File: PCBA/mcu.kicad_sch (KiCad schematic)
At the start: 13 parts, among them U201 BL604, Y201 40MHz

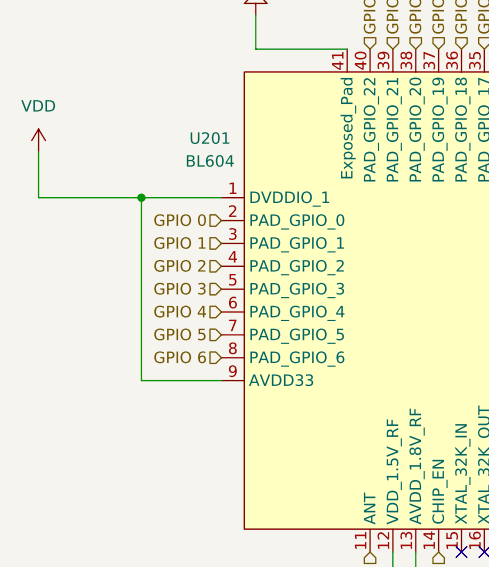
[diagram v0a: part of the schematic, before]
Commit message: Programming uart added
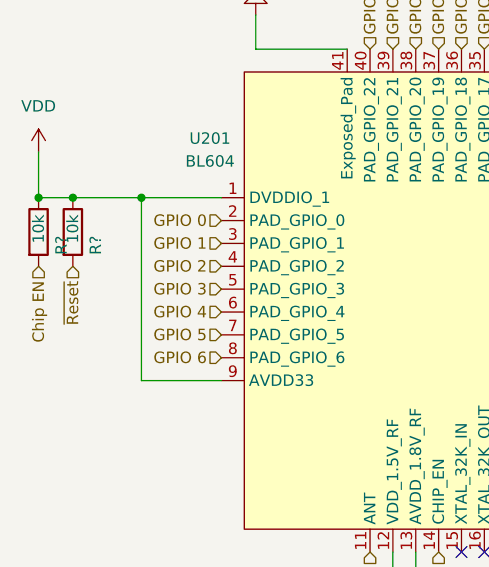
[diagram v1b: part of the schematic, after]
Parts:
- added R? (x2): 10k, Resistor_SMD:R_0603_1608Metric, symbol Device:R
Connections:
- net AVDD33: now also R?.1, R?.1
- net Chip EN: now also R?.2
- net ~{Reset}: now also R?.2
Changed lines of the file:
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@@
   (junction (at 101.6 80.01) (diameter 0) (color 0 0 0 0)
+  )
+  (junction (at 90.17 80.01) (diameter 0) (color 0 0 0 0)
+  )
+  (junction (at 93.98 80.01) (diameter 0) (color 0 0 0 0)
   )
   (junction (at 185.42 114.3) (diameter 0) (color 0 0 0 0)
@@
     (stroke (width 0) (type default) (color 0 0 0 0))
   )
-  (wire (pts (xy 101.6 80.01) (xy 90.17 80.01))
+  (wire (pts (xy 101.6 80.01) (xy 93.98 80.01))
     (stroke (width 0) (type default) (color 0 0 0 0))
   )
@@
   )
   (wire (pts (xy 154.94 63.5) (xy 154.94 55.88))
+    (stroke (width 0) (type default) (color 0 0 0 0))
+  )
+  (wire (pts (xy 93.98 80.01) (xy 90.17 80.01))
     (stroke (width 0) (type default) (color 0 0 0 0))
   )
@@
     (effects (font (size 1.27 1.27)) (justify right))
   )
+  (hierarchical_label "Chip EN" (shape input) (at 90.17 87.63 270)
+    (effects (font (size 1.27 1.27)) (justify right))
+  )
   (hierarchical_label "GPIO 13" (shape input) (at 166.37 87.63 0)
     (effects (font (size 1.27 1.27)) (justify left))
@@
   (hierarchical_label "GPIO 17" (shape input) (at 139.7 63.5 90)
     (effects (font (size 1.27 1.27)) (justify left))
+  )
+  (hierarchical_label "~{Reset}" (shape input) (at 93.98 87.63 270)
+    (effects (font (size 1.27 1.27)) (justify right))
   )
   (hierarchical_label "GPIO 9" (shape input) (at 166.37 97.79 0)
@@
     )
     (property "Datasheet" "~" (id 3) (at 151.13 55.88 0)
+      (effects (font (size 1.27 1.27)) hide)
+    )
+    (pin "1")
+    (pin "2")
+  )
+  (symbol (lib_id "Device:R") (at 93.98 83.82 0) (unit 1)
+    (in_bom yes) (on_board yes)
+    (property "Reference" "R?" (id 0) (at 96.52 86.36 90)
+      (effects (font (size 1.27 1.27)) (justify left))
+    )
+    (property "Value" "10k" (id 1) (at 93.98 85.09 90)
+      (effects (font (size 1.27 1.27)) (justify left))
+    )
+    (property "Footprint" "Resistor_SMD:R_0603_1608Metric" (id 2) (at 92.202 83.82 90)
+      (effects (font (size 1.27 1.27)) hide)
+    )
+    (property "Datasheet" "~" (id 3) (at 93.98 83.82 0)
       (effects (font (size 1.27 1.27)) hide)
     )
@@
       (effects (font (size 1.27 1.27)) hide)
     )
+    (pin "1")
+    (pin "2")
+  )
+  (symbol (lib_id "Device:R") (at 90.17 83.82 0) (unit 1)
+    (in_bom yes) (on_board yes)
+    (property "Reference" "R?" (id 0) (at 92.71 86.36 90)
+      (effects (font (size 1.27 1.27)) (justify left))
+    )
+    (property "Value" "10k" (id 1) (at 90.17 85.09 90)
+      (effects (font (size 1.27 1.27)) (justify left))
+    )
+    (property "Footprint" "Resistor_SMD:R_0603_1608Metric" (id 2) (at 88.392 83.82 90)
+      (effects (font (size 1.27 1.27)) hide)
+    )
+    (property "Datasheet" "~" (id 3) (at 90.17 83.82 0)
+      (effects (font (size 1.27 1.27)) hide)
+    )

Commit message: More schematics
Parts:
- gave numbers to parts that had none: 2
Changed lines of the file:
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@@
   (symbol (lib_id "Device:R") (at 93.98 83.82 0) (unit 1)
     (in_bom yes) (on_board yes)
-    (property "Reference" "R?" (id 0) (at 96.52 86.36 90)
+    (property "Reference" "R203" (id 0) (at 96.52 86.36 90)
       (effects (font (size 1.27 1.27)) (justify left))
     )
@@
   (symbol (lib_id "Device:R") (at 90.17 83.82 0) (unit 1)
     (in_bom yes) (on_board yes)
-    (property "Reference" "R?" (id 0) (at 92.71 86.36 90)
-      (effects (font (size 1.27 1.27)) (justify left))
-    )
+    (property "Reference" "R202" (id 0) (at 92.71 86.36 90)
+      (effects (font (size 1.27 1.27)) (justify left))
+    )

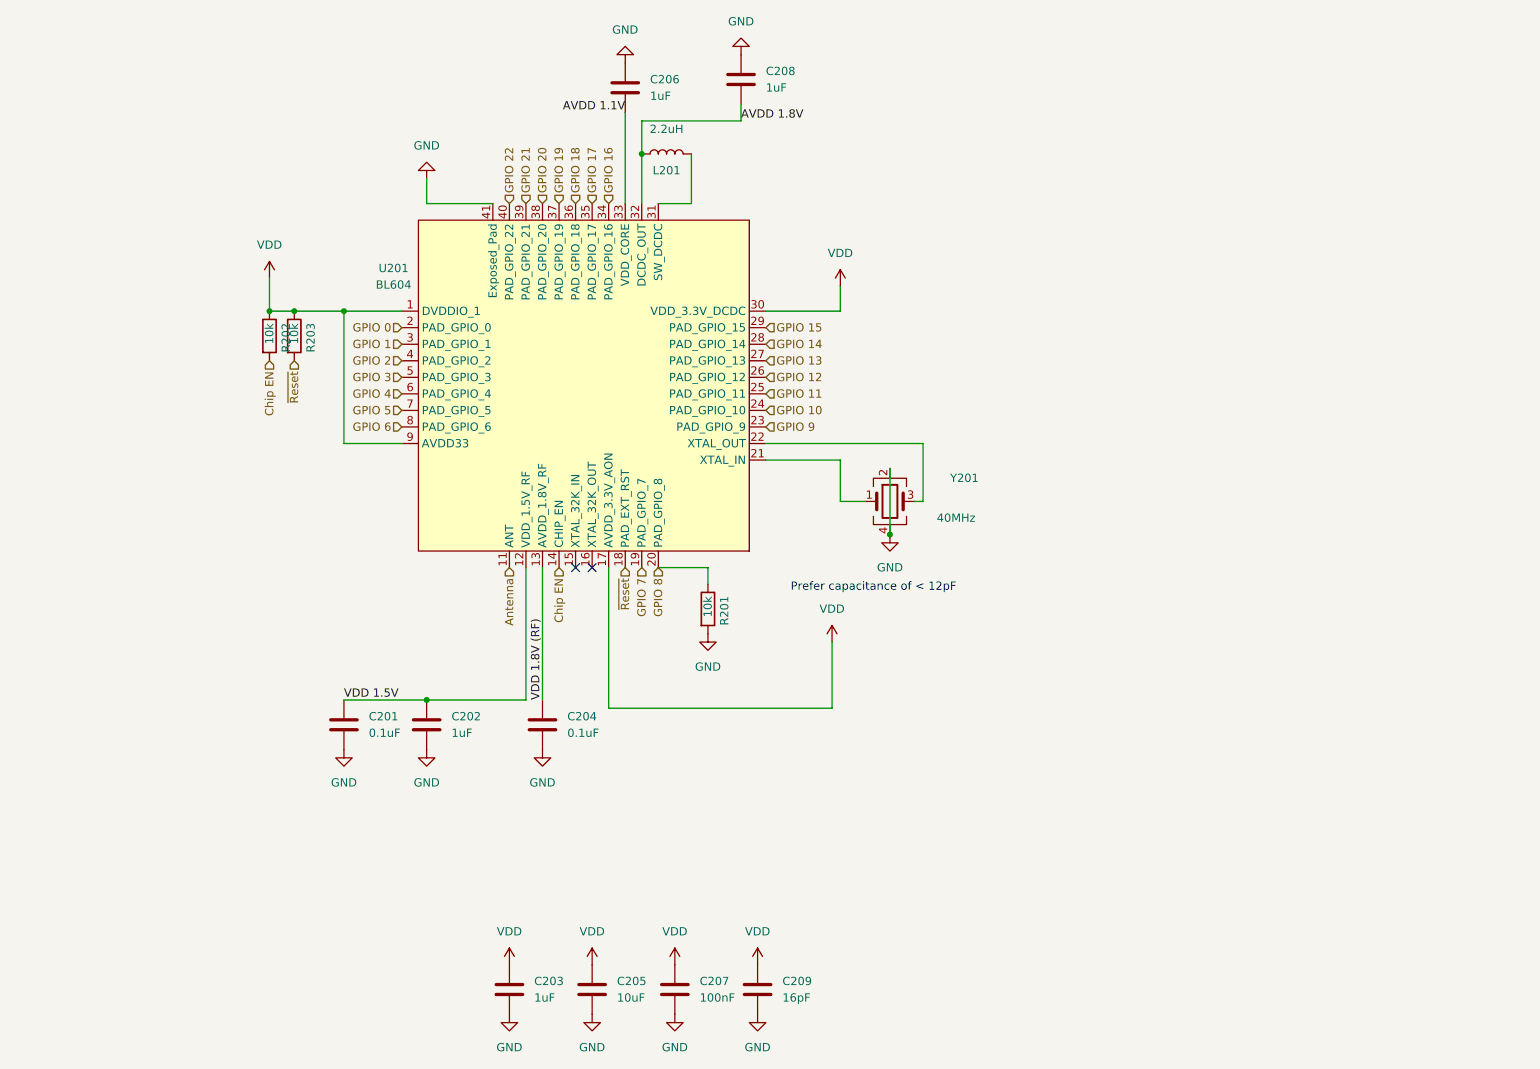
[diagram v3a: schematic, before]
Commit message: Update schematic pinmap bl706
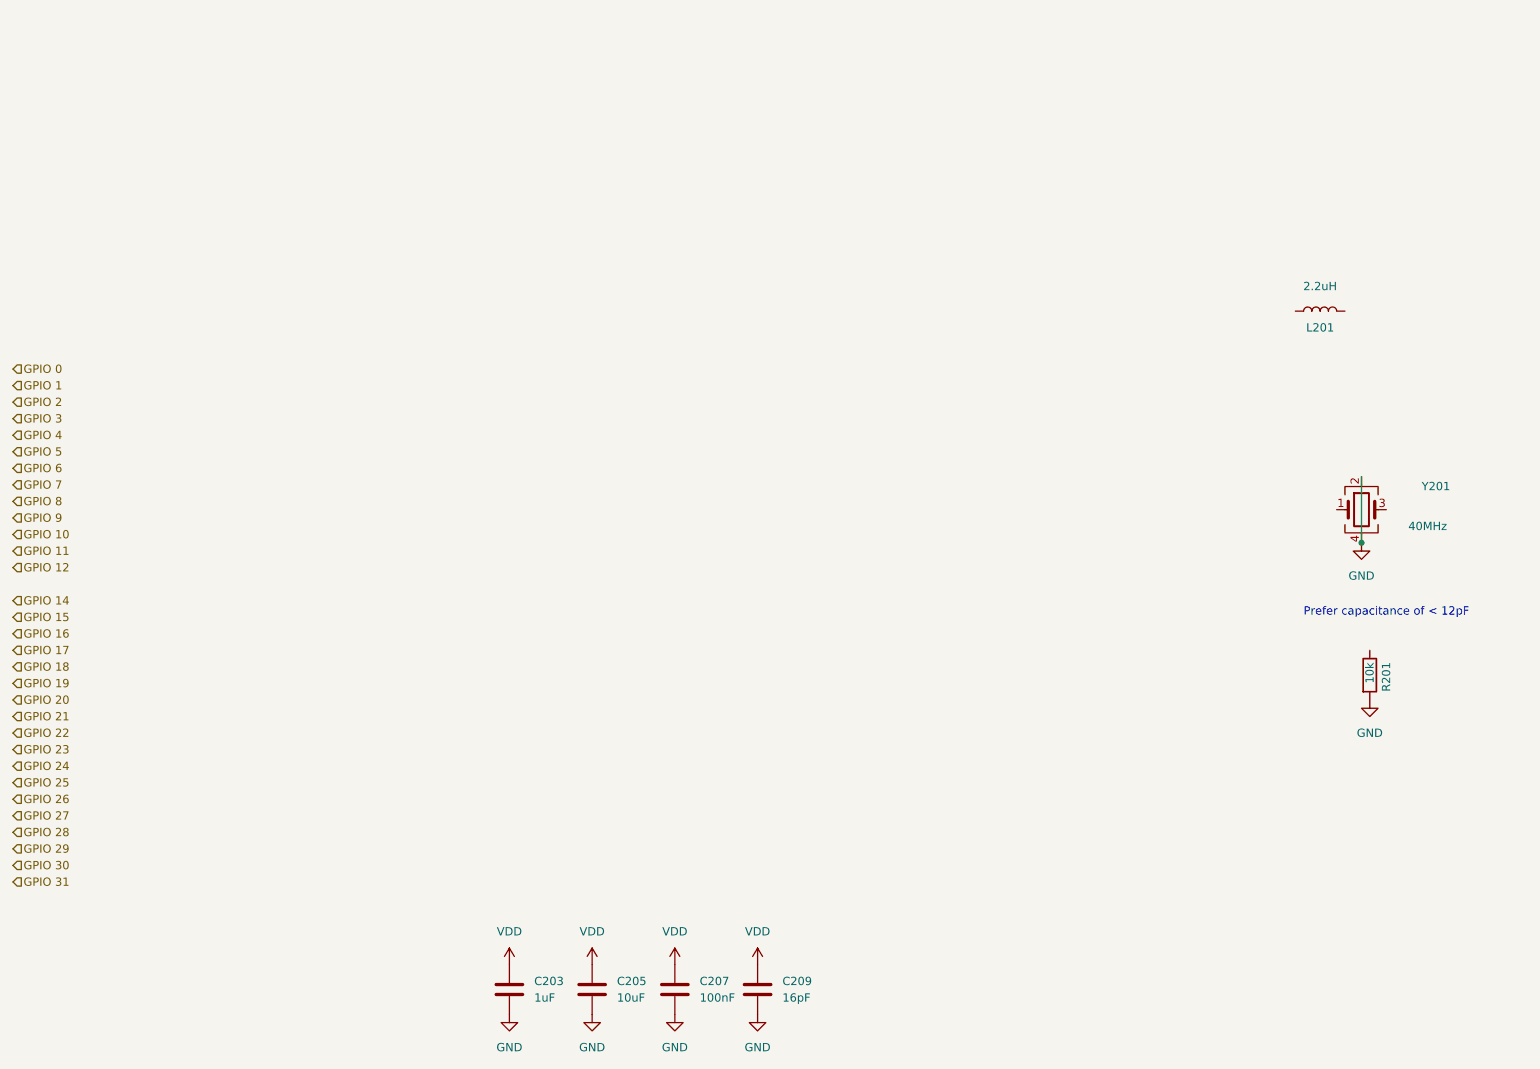
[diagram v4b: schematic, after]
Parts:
- removed C201, C204: 0.1uF, Capacitor_SMD:C_0603_1608Metric, symbol Device:C
- removed C202, C206, C208: 1uF, Capacitor_SMD:C_0603_1608Metric, symbol Device:C
- removed R202, R203: 10k, Resistor_SMD:R_0603_1608Metric, symbol Device:R
- removed U201: BL604, Package_DFN_QFN:QFN-40-1EP_5x5mm_P0.4mm_EP3.6x3.6mm, symbol BL60x:BL604
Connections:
- net GPIO 8: no longer R201.1
- net AVDD 1.8V: no longer names the net of L201.1
- net AVDD33 renamed VDD
- no-connect marks 2 -> 0
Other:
- moved on the sheet: L201, R201, Y201

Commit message: Rough outline
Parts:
- added AE201: KH2012F245C04, Resistor_SMD:R_0805_2012Metric, symbol Device:Antenna_Chip
- added C201, C202, C204, C208: 1uF, Capacitor_SMD:C_0603_1608Metric, symbol Device:C
- added C206, C210: 100nF, Capacitor_SMD:C_0603_1608Metric, symbol Device:C
- added C211, C212: -, Capacitor_SMD:C_0603_1608Metric, symbol Device:C
- added C213: 0.1uF, Capacitor_SMD:C_0603_1608Metric, symbol Device:C
- added R202: 0, Resistor_SMD:R_0603_1608Metric, symbol Device:R
- added U201: BL706, Package_DFN_QFN:QFN-48-1EP_6x6mm_P0.4mm_EP4.2x4.2mm, symbol bl70x:BL706
- L201: footprint (none) -> Inductor_SMD:L_Wuerth_MAPI-3010
- Y201: footprint (none) -> Crystal:Crystal_SMD_2016-4Pin_2.0x1.6mm
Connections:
- net GND: now also AE201.1 (FEED), C201.2, C202.2, C211.2, C212.2, C213.2; no longer R201.2
- net GPIO 0: now also U201.1 (PAD_GPIO_0)
- net GPIO 1: now also U201.2 (PAD_GPIO_1)
- net GPIO 10: now also U201.16 (PAD_GPIO_10)
- net GPIO 11: now also U201.17 (PAD_GPIO_11)
- net GPIO 12: now also U201.18 (PAD_GPIO_12)
- net GPIO 14: now also U201.29 (PAD_GPIO_14)
- net GPIO 15: now also U201.30 (PAD_GPIO_15)
- net GPIO 16: now also U201.31 (PAD_GPIO_16)
- net GPIO 17: now also U201.32 (PAD_GPIO_17)
- net GPIO 18: now also U201.33 (PAD_GPIO_18)
- net GPIO 19: now also U201.34 (PAD_GPIO_19)
- net GPIO 2: now also U201.3 (PAD_GPIO_2)
- net GPIO 20: now also U201.35 (PAD_GPIO_20)
- net GPIO 21: now also U201.37 (PAD_GPIO_21)
- net GPIO 22: now also U201.38 (PAD_GPIO_22)
- net GPIO 23: now also U201.39 (PAD_GPIO_23)
- net GPIO 24: now also U201.40 (PAD_GPIO_24)
- net GPIO 25: now also U201.41 (PAD_GPIO_25)
- net GPIO 26: now also U201.42 (PAD_GPIO_26)
- net GPIO 27: now also U201.43 (PAD_GPIO_27)
- net GPIO 28: now also U201.44 (PAD_GPIO_28)
- net GPIO 29: now also U201.45 (PAD_GPIO_29)
- net GPIO 3: now also U201.4 (PAD_GPIO_3)
- net GPIO 30: now also U201.46 (PAD_GPIO_30)
- net GPIO 31: now also U201.47 (PAD_GPIO_31)
- net GPIO 4: now also U201.5 (PAD_GPIO_4)
- net GPIO 5: now also U201.6 (PAD_GPIO_5)
- net GPIO 6: now also U201.7 (PAD_GPIO_6)
- net GPIO 7: now also U201.8 (PAD_GPIO_7)
- net GPIO 8: now also U201.9 (PAD_GPIO_8)
- net GPIO 9: now also U201.15 (PAD_GPIO_9)
- net VDD: now also R201.2, C213.1, U201.14 (VDDIO_2), U201.21 (AVDD33_AON), U201.24 (AVDD33_PA), U201.36 (VDDIO_3), U201.48 (VDDIO_1)
- net ~{RESET}: now reaches R201.1
- net ~{RESET}: now also U201.22 (PU_CHIP)
- net at L201.1: now also U201.12 (DCDC_OUT)
- net at L201.2: now also U201.13 (SW_DCDC)
- net at Y201.1: now also U201.27 (XTAL_HF_IN)
- net at Y201.3: now also U201.28 (XTAL_HF_OUT)
- new net: C211.1, R202.1, U201.23 (ANT)
- new net: AE201.2 (PCB_Trace), C212.1, R202.2
- new net: C202.1, U201.11 (VDDCORE)
- new net: C204.1, C206.1, U201.25 (AVDD15)
- new net: C204.2, C206.2, C208.2, C210.2
- new net: C201.1, U201.10 (VDDBUS_USB)
- new net: C208.1, C210.1, U201.26 (AVDD_RF)
- no-connect marks 0 -> 2
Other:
- moved on the sheet: L201, R201, Y201

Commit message: More rough placement
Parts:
- L201: footprint Inductor_SMD:L_Wuerth_MAPI-3010 -> Inductor_SMD:L_0805_2012Metric
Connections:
- net GND: now also C204.2, C206.2, C208.2, C210.2
- net RF: now reaches C211.1, R202.1, U201.23 (ANT)
- net ANT: now reaches AE201.2 (PCB_Trace), C212.1, R202.2
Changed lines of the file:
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@@
   (junction (at 200.66 121.92) (diameter 0) (color 0 0 0 0)
+  )
+  (junction (at 209.55 121.92) (diameter 0) (color 0 0 0 0)
   )
   (junction (at 171.45 129.54) (diameter 0) (color 0 0 0 0)
@@
     (stroke (width 0) (type default) (color 0 0 0 0))
   )
-  (wire (pts (xy 200.66 121.92) (xy 215.9 121.92))
+  (wire (pts (xy 200.66 121.92) (xy 209.55 121.92))
     (stroke (width 0) (type default) (color 0 0 0 0))
   )
@@
   )
   (wire (pts (xy 175.26 129.54) (xy 171.45 129.54))
+    (stroke (width 0) (type default) (color 0 0 0 0))
+  )
+  (wire (pts (xy 209.55 121.92) (xy 215.9 121.92))
     (stroke (width 0) (type default) (color 0 0 0 0))
   )
@@
   (text "Prefer capacitance of < 12pF" (at 236.22 109.22 180)
     (effects (font (size 1.27 1.27)) (justify right bottom))
+  )
+  (label "ANT" (at 182.88 129.54 0)
+    (effects (font (size 1.27 1.27)) (justify left bottom))
+  )
+  (label "RF" (at 171.45 129.54 0)
+    (effects (font (size 1.27 1.27)) (justify left bottom))
   )
   (hierarchical_label "GPIO 18" (shape input) (at 184.15 90.17 0)
@@
     (property "Reference" "L201" (id 0) (at 107.95 129.54 90))
     (property "Value" "2.2uH" (id 1) (at 107.95 123.19 90))
-    (property "Footprint" "Inductor_SMD:L_Wuerth_MAPI-3010" (id 2) (at 107.95 127 0)
-      (effects (font (size 1.27 1.27)) hide)
-    )
+    (property "Footprint" "Inductor_SMD:L_0805_2012Metric" (id 2) (at 107.95 127 0)
+      (effects (font (size 1.27 1.27)) hide)
+    )
